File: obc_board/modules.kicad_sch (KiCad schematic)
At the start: 26 parts, among them J10 FSI-110-03-X-D-AD-SD-K-TR, J9 FSI-110-03-X-D-AD-SD-K-TR, U11 LTC4304CMSTRPBF, U12 LTC4304CMSTRPBF

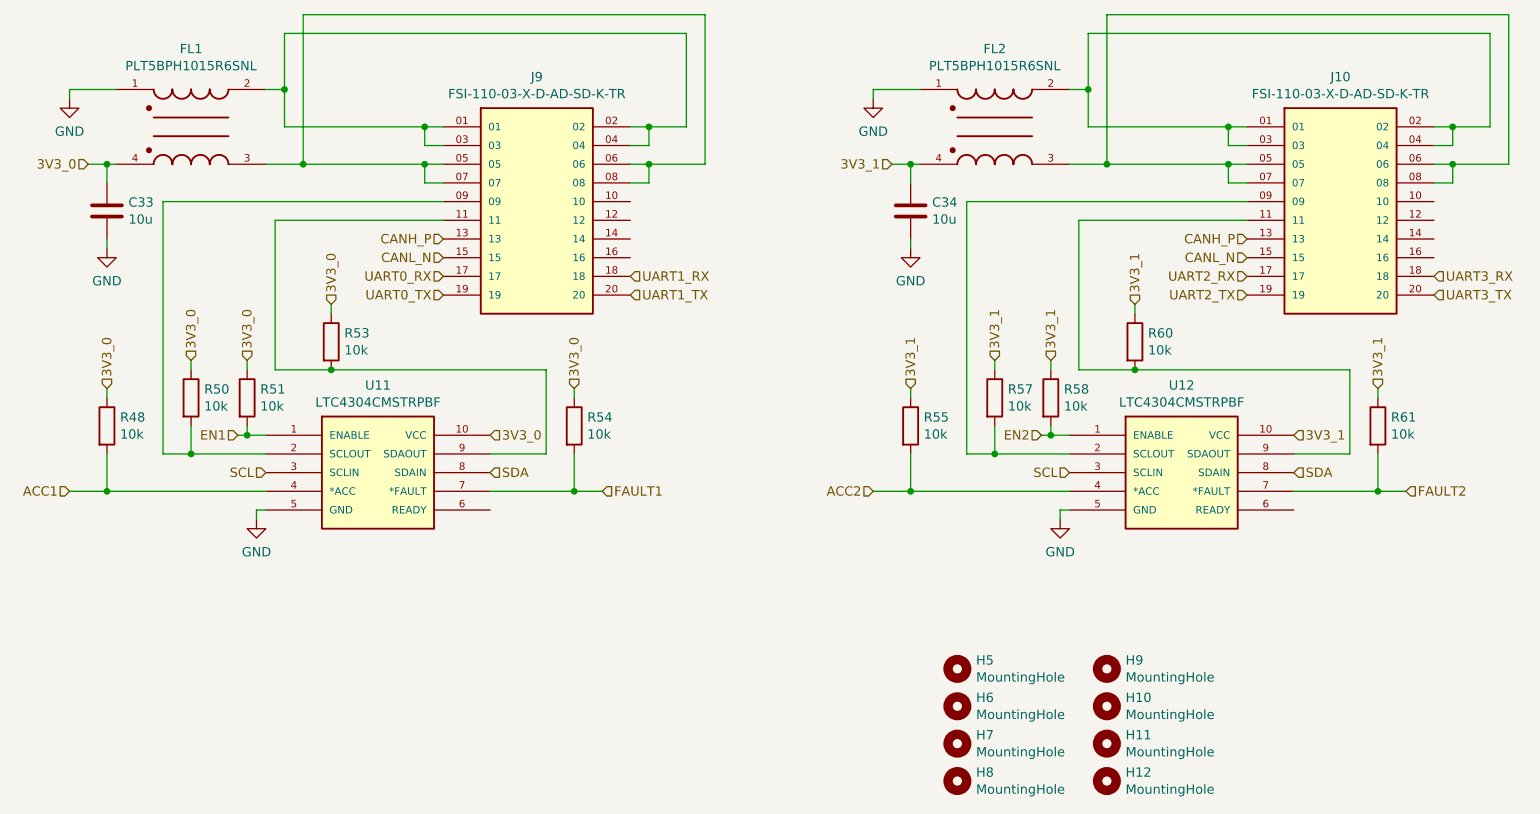
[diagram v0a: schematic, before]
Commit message: changed magnetorquer driver IC and changed power switch IC
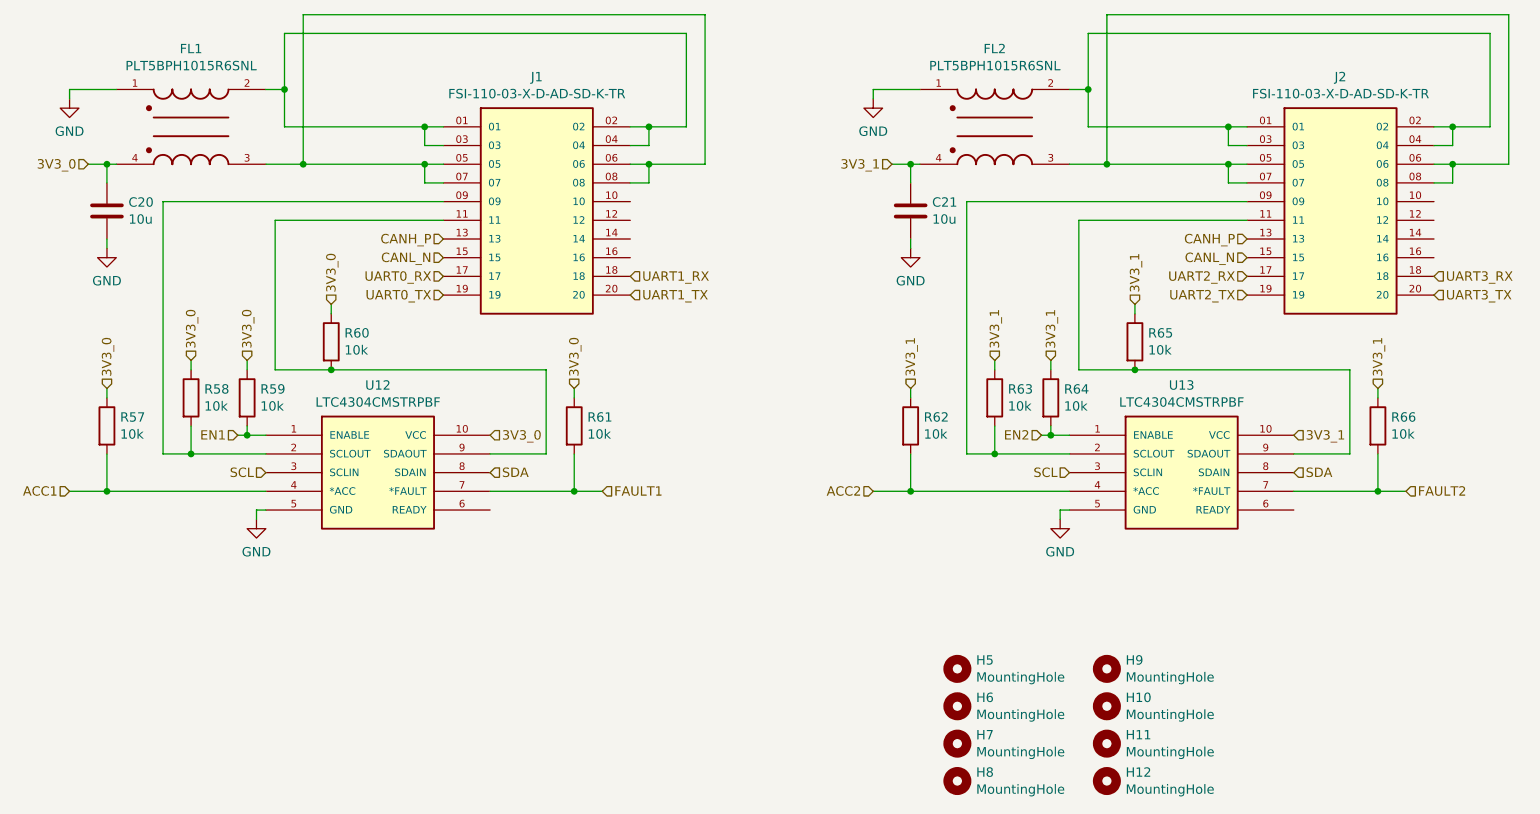
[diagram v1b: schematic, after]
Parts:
- renumbered C33 to C20, C34 to C21, J9 to J1, J10 to J2, R48 to R57, R50 to R58, R51 to R59, R53 to R60, R54 to R61, R55 to R62, R57 to R63, R58 to R64, R60 to R65, R61 to R66, U11 to U12, U12 to U13
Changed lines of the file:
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@@
   (symbol (lib_id "cubesat_obc_lib:FSI-110-03-X-D-AD-SD-K-TR") (at 115.57 76.2 0) (unit 1)
     (in_bom yes) (on_board yes)
-    (property "Reference" "J9" (id 0) (at 115.57 56.7182 0))
+    (property "Reference" "J1" (id 0) (at 115.57 56.7182 0))
     (property "Value" "FSI-110-03-X-D-AD-SD-K-TR" (id 1) (at 115.57 59.0296 0))
     (property "Footprint" "SAMTEC_FSI-110-03-X-D-AD-SD-K-TR" (id 2) (at 115.57 76.2 0)
@@
   (symbol (lib_id "Device:C") (at 57.15 74.93 0) (unit 1)
     (in_bom yes) (on_board yes)
-    (property "Reference" "C33" (id 0) (at 60.071 73.7616 0)
+    (property "Reference" "C20" (id 0) (at 60.071 73.7616 0)
       (effects (font (size 1.27 1.27)) (justify left))
     )
@@
   (symbol (lib_id "cubesat_obc_lib:LTC4304CMSTRPBF") (at 54.61 106.68 0) (unit 1)
     (in_bom yes) (on_board yes)
-    (property "Reference" "U11" (id 0) (at 93.98 98.6282 0))
+    (property "Reference" "U12" (id 0) (at 93.98 98.6282 0))
     (property "Value" "LTC4304CMSTRPBF" (id 1) (at 93.98 100.9396 0))
     (property "Footprint" "MSOP-10_MS" (id 2) (at 78.74 105.41 0)
@@
   (symbol (lib_id "Device:R") (at 76.2 100.33 0) (unit 1)
     (in_bom yes) (on_board yes)
-    (property "Reference" "R51" (id 0) (at 77.978 99.1616 0)
+    (property "Reference" "R59" (id 0) (at 77.978 99.1616 0)
       (effects (font (size 1.27 1.27)) (justify left))
     )
@@
   (symbol (lib_id "Device:R") (at 57.15 104.14 0) (unit 1)
     (in_bom yes) (on_board yes)
-    (property "Reference" "R48" (id 0) (at 58.928 102.9716 0)
+    (property "Reference" "R57" (id 0) (at 58.928 102.9716 0)
       (effects (font (size 1.27 1.27)) (justify left))
     )
@@
   (symbol (lib_id "Device:R") (at 120.65 104.14 0) (unit 1)
     (in_bom yes) (on_board yes)
-    (property "Reference" "R54" (id 0) (at 122.428 102.9716 0)
+    (property "Reference" "R61" (id 0) (at 122.428 102.9716 0)
       (effects (font (size 1.27 1.27)) (justify left))
     )
@@
   (symbol (lib_id "Device:R") (at 87.63 92.71 0) (unit 1)
     (in_bom yes) (on_board yes)
-    (property "Reference" "R53" (id 0) (at 89.408 91.5416 0)
+    (property "Reference" "R60" (id 0) (at 89.408 91.5416 0)
       (effects (font (size 1.27 1.27)) (justify left))
     )
@@
   (symbol (lib_id "Device:R") (at 68.58 100.33 0) (unit 1)
     (in_bom yes) (on_board yes)
-    (property "Reference" "R50" (id 0) (at 70.358 99.1616 0)
+    (property "Reference" "R58" (id 0) (at 70.358 99.1616 0)
       (effects (font (size 1.27 1.27)) (justify left))
     )
@@
   (symbol (lib_id "cubesat_obc_lib:FSI-110-03-X-D-AD-SD-K-TR") (at 224.79 76.2 0) (unit 1)
     (in_bom yes) (on_board yes)
-    (property "Reference" "J10" (id 0) (at 224.79 56.7182 0))
+    (property "Reference" "J2" (id 0) (at 224.79 56.7182 0))
     (property "Value" "FSI-110-03-X-D-AD-SD-K-TR" (id 1) (at 224.79 59.0296 0))
     (property "Footprint" "SAMTEC_FSI-110-03-X-D-AD-SD-K-TR" (id 2) (at 224.79 76.2 0)
@@
   (symbol (lib_id "Device:C") (at 166.37 74.93 0) (unit 1)
     (in_bom yes) (on_board yes)
-    (property "Reference" "C34" (id 0) (at 169.291 73.7616 0)
+    (property "Reference" "C21" (id 0) (at 169.291 73.7616 0)
       (effects (font (size 1.27 1.27)) (justify left))
     )
@@
   (symbol (lib_id "cubesat_obc_lib:LTC4304CMSTRPBF") (at 163.83 106.68 0) (unit 1)
     (in_bom yes) (on_board yes)
-    (property "Reference" "U12" (id 0) (at 203.2 98.6282 0))
+    (property "Reference" "U13" (id 0) (at 203.2 98.6282 0))
     (property "Value" "LTC4304CMSTRPBF" (id 1) (at 203.2 100.9396 0))
     (property "Footprint" "MSOP-10_MS" (id 2) (at 187.96 105.41 0)
@@
   (symbol (lib_id "Device:R") (at 185.42 100.33 0) (unit 1)
     (in_bom yes) (on_board yes)
-    (property "Reference" "R58" (id 0) (at 187.198 99.1616 0)
+    (property "Reference" "R64" (id 0) (at 187.198 99.1616 0)
       (effects (font (size 1.27 1.27)) (justify left))
     )
@@
   (symbol (lib_id "Device:R") (at 166.37 104.14 0) (unit 1)
     (in_bom yes) (on_board yes)
-    (property "Reference" "R55" (id 0) (at 168.148 102.9716 0)
+    (property "Reference" "R62" (id 0) (at 168.148 102.9716 0)
       (effects (font (size 1.27 1.27)) (justify left))
     )
@@
   (symbol (lib_id "Device:R") (at 229.87 104.14 0) (unit 1)
     (in_bom yes) (on_board yes)
-    (property "Reference" "R61" (id 0) (at 231.648 102.9716 0)
+    (property "Reference" "R66" (id 0) (at 231.648 102.9716 0)
       (effects (font (size 1.27 1.27)) (justify left))
     )
@@
   (symbol (lib_id "Device:R") (at 196.85 92.71 0) (unit 1)
     (in_bom yes) (on_board yes)
-    (property "Reference" "R60" (id 0) (at 198.628 91.5416 0)
+    (property "Reference" "R65" (id 0) (at 198.628 91.5416 0)
       (effects (font (size 1.27 1.27)) (justify left))
     )
@@
   (symbol (lib_id "Device:R") (at 177.8 100.33 0) (unit 1)
     (in_bom yes) (on_board yes)
-    (property "Reference" "R57" (id 0) (at 179.578 99.1616 0)
+    (property "Reference" "R63" (id 0) (at 179.578 99.1616 0)
       (effects (font (size 1.27 1.27)) (justify left))
     )
@@
   (symbol (lib_id "power:GND") (at 166.37 80.01 0) (unit 1)
     (in_bom yes) (on_board yes) (fields_autoplaced)
-    (property "Reference" "#PWR?" (id 0) (at 166.37 86.36 0)
+    (property "Reference" "#PWR038" (id 0) (at 166.37 86.36 0)
       (effects (font (size 1.27 1.27)) hide)
     )
@@
   (symbol (lib_id "power:GND") (at 57.15 80.01 0) (unit 1)
     (in_bom yes) (on_board yes) (fields_autoplaced)
-    (property "Reference" "#PWR?" (id 0) (at 57.15 86.36 0)
+    (property "Reference" "#PWR035" (id 0) (at 57.15 86.36 0)
       (effects (font (size 1.27 1.27)) hide)
     )
@@
   (symbol (lib_id "power:GND") (at 77.47 116.84 0) (unit 1)
     (in_bom yes) (on_board yes) (fields_autoplaced)
-    (property "Reference" "#PWR?" (id 0) (at 77.47 123.19 0)
+    (property "Reference" "#PWR036" (id 0) (at 77.47 123.19 0)
       (effects (font (size 1.27 1.27)) hide)
     )
@@
   (symbol (lib_id "power:GND") (at 52.07 59.69 0) (unit 1)
     (in_bom yes) (on_board yes) (fields_autoplaced)
-    (property "Reference" "#PWR?" (id 0) (at 52.07 66.04 0)
+    (property "Reference" "#PWR034" (id 0) (at 52.07 66.04 0)
       (effects (font (size 1.27 1.27)) hide)
     )
@@
   (symbol (lib_id "power:GND") (at 186.69 116.84 0) (unit 1)
     (in_bom yes) (on_board yes) (fields_autoplaced)
-    (property "Reference" "#PWR?" (id 0) (at 186.69 123.19 0)
+    (property "Reference" "#PWR039" (id 0) (at 186.69 123.19 0)
       (effects (font (size 1.27 1.27)) hide)
     )
@@
   (symbol (lib_id "power:GND") (at 161.29 59.69 0) (unit 1)
     (in_bom yes) (on_board yes) (fields_autoplaced)
-    (property "Reference" "#PWR?" (id 0) (at 161.29 66.04 0)
-      (effects (font (size 1.27 1.27)) hide)
-    )
+    (property "Reference" "#PWR037" (id 0) (at 161.29 66.04 0)
+      (effects (font (size 1.27 1.27)) hide)
+    )

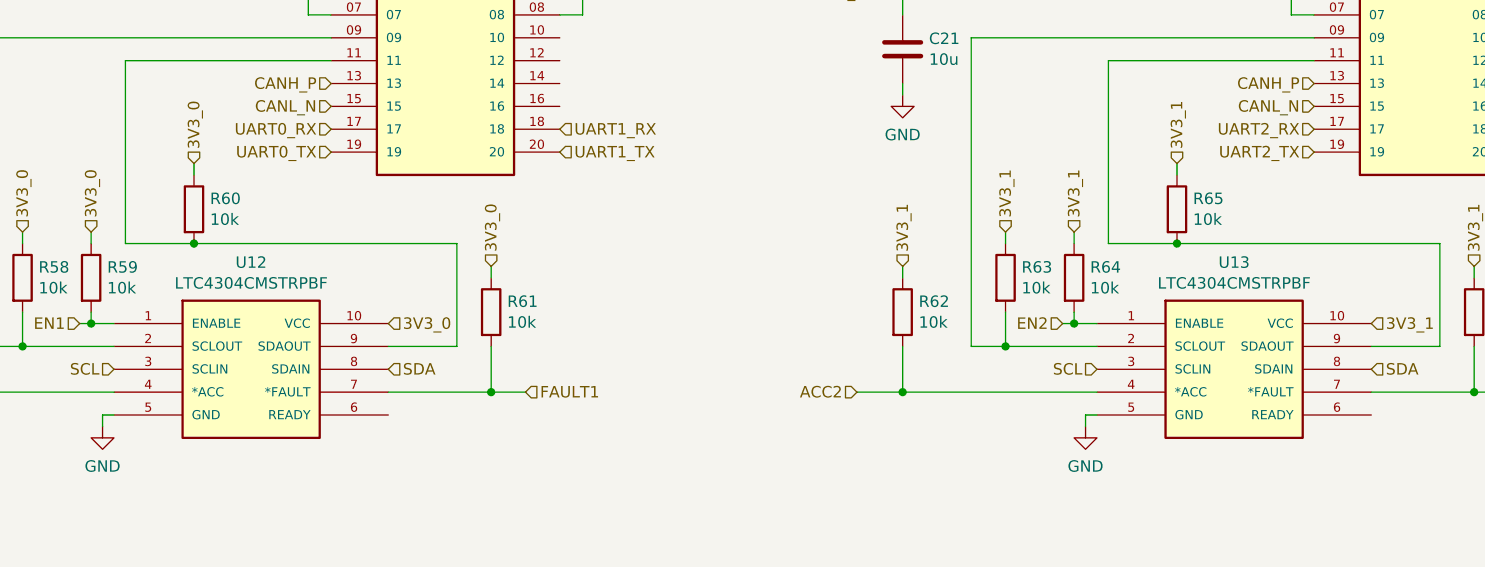
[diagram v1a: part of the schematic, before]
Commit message: updated digikey part numbers and footprints
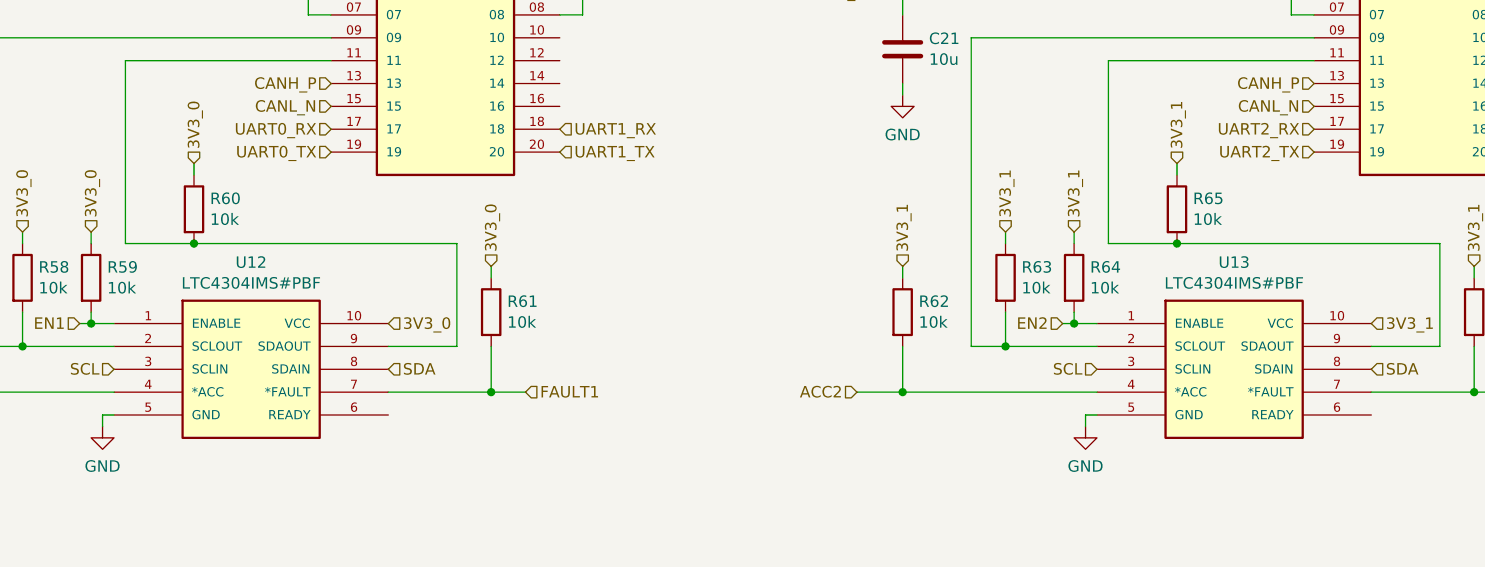
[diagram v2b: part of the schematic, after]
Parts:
- C20, C21: Digikey Part Number 311-1952-1-ND -> 399-7012-1-ND
- R57, R58, R59, R60, R61, R62, R63, R64, R65, R66: Digikey Part Number 311-10.0KLRCT-ND -> YAG3436CT-ND
- U12, U13: value LTC4304CMSTRPBF -> LTC4304IMS#PBF; Digikey Part Number LTC4304CMS#PBF-ND -> LTC4304IMS#PBF-ND
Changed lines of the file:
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@@
       (effects (font (size 1.27 1.27)) hide)
     )
-    (property "Digikey Part Number" "311-1952-1-ND" (id 4) (at 57.15 74.93 0)
+    (property "Digikey Part Number" "399-7012-1-ND" (id 4) (at 57.15 74.93 0)
       (effects (font (size 1.27 1.27)) hide)
     )
@@
     (in_bom yes) (on_board yes)
     (property "Reference" "U12" (id 0) (at 93.98 98.6282 0))
-    (property "Value" "LTC4304CMSTRPBF" (id 1) (at 93.98 100.9396 0))
+    (property "Value" "LTC4304IMS#PBF" (id 1) (at 93.98 100.9396 0))
     (property "Footprint" "MSOP-10_MS" (id 2) (at 78.74 105.41 0)
       (effects (font (size 1.27 1.27)) (justify left bottom) hide)
     )
-    (property "Datasheet" "ltc4304cms#trpbf" (id 3) (at 78.74 105.41 0)
+    (property "Datasheet" "https://www.analog.com/media/en/technical-documentation/data-sheets/4304fa.pdf" (id 3) (at 78.74 105.41 0)
       (effects (font (size 1.27 1.27)) (justify left bottom) hide)
     )
@@
       (effects (font (size 1.27 1.27)) (justify left bottom) hide)
     )
-    (property "Digikey Part Number" "LTC4304CMS#PBF-ND" (id 5) (at 54.61 106.68 0)
+    (property "Digikey Part Number" "LTC4304IMS#PBF-ND" (id 5) (at 54.61 106.68 0)
       (effects (font (size 1.27 1.27)) hide)
     )
@@
       (effects (font (size 1.27 1.27)) hide)
     )
-    (property "Digikey Part Number" "311-10.0KLRCT-ND" (id 4) (at 76.2 100.33 0)
+    (property "Digikey Part Number" "YAG3436CT-ND" (id 4) (at 76.2 100.33 0)
       (effects (font (size 1.27 1.27)) hide)
     )
@@
       (effects (font (size 1.27 1.27)) hide)
     )
-    (property "Digikey Part Number" "311-10.0KLRCT-ND" (id 4) (at 57.15 104.14 0)
+    (property "Digikey Part Number" "YAG3436CT-ND" (id 4) (at 57.15 104.14 0)
       (effects (font (size 1.27 1.27)) hide)
     )
@@
       (effects (font (size 1.27 1.27)) hide)
     )
-    (property "Digikey Part Number" "311-10.0KLRCT-ND" (id 4) (at 120.65 104.14 0)
+    (property "Digikey Part Number" "YAG3436CT-ND" (id 4) (at 120.65 104.14 0)
       (effects (font (size 1.27 1.27)) hide)
     )
@@
       (effects (font (size 1.27 1.27)) hide)
     )
-    (property "Digikey Part Number" "311-10.0KLRCT-ND" (id 4) (at 87.63 92.71 0)
+    (property "Digikey Part Number" "YAG3436CT-ND" (id 4) (at 87.63 92.71 0)
       (effects (font (size 1.27 1.27)) hide)
     )
@@
       (effects (font (size 1.27 1.27)) hide)
     )
-    (property "Digikey Part Number" "311-10.0KLRCT-ND" (id 4) (at 68.58 100.33 0)
+    (property "Digikey Part Number" "YAG3436CT-ND" (id 4) (at 68.58 100.33 0)
       (effects (font (size 1.27 1.27)) hide)
     )
@@
       (effects (font (size 1.27 1.27)) hide)
     )
-    (property "Digikey Part Number" "311-1952-1-ND" (id 4) (at 166.37 74.93 0)
+    (property "Digikey Part Number" "399-7012-1-ND" (id 4) (at 166.37 74.93 0)
       (effects (font (size 1.27 1.27)) hide)
     )
@@
     (in_bom yes) (on_board yes)
     (property "Reference" "U13" (id 0) (at 203.2 98.6282 0))
-    (property "Value" "LTC4304CMSTRPBF" (id 1) (at 203.2 100.9396 0))
+    (property "Value" "LTC4304IMS#PBF" (id 1) (at 203.2 100.9396 0))
     (property "Footprint" "MSOP-10_MS" (id 2) (at 187.96 105.41 0)
       (effects (font (size 1.27 1.27)) (justify left bottom) hide)
     )
-    (property "Datasheet" "ltc4304cms#trpbf" (id 3) (at 187.96 105.41 0)
+    (property "Datasheet" "https://www.analog.com/media/en/technical-documentation/data-sheets/4304fa.pdf" (id 3) (at 187.96 105.41 0)
       (effects (font (size 1.27 1.27)) (justify left bottom) hide)
     )
@@
       (effects (font (size 1.27 1.27)) (justify left bottom) hide)
     )
-    (property "Digikey Part Number" "LTC4304CMS#PBF-ND" (id 5) (at 163.83 106.68 0)
+    (property "Digikey Part Number" "LTC4304IMS#PBF-ND" (id 5) (at 163.83 106.68 0)
       (effects (font (size 1.27 1.27)) hide)
     )
@@
       (effects (font (size 1.27 1.27)) hide)
     )
-    (property "Digikey Part Number" "311-10.0KLRCT-ND" (id 4) (at 185.42 100.33 0)
+    (property "Digikey Part Number" "YAG3436CT-ND" (id 4) (at 185.42 100.33 0)
       (effects (font (size 1.27 1.27)) hide)
     )
@@
       (effects (font (size 1.27 1.27)) hide)
     )
-    (property "Digikey Part Number" "311-10.0KLRCT-ND" (id 4) (at 166.37 104.14 0)
+    (property "Digikey Part Number" "YAG3436CT-ND" (id 4) (at 166.37 104.14 0)
       (effects (font (size 1.27 1.27)) hide)
     )
@@
       (effects (font (size 1.27 1.27)) hide)
     )
-    (property "Digikey Part Number" "311-10.0KLRCT-ND" (id 4) (at 229.87 104.14 0)
+    (property "Digikey Part Number" "YAG3436CT-ND" (id 4) (at 229.87 104.14 0)
       (effects (font (size 1.27 1.27)) hide)
     )
@@
       (effects (font (size 1.27 1.27)) hide)
     )
-    (property "Digikey Part Number" "311-10.0KLRCT-ND" (id 4) (at 196.85 92.71 0)
+    (property "Digikey Part Number" "YAG3436CT-ND" (id 4) (at 196.85 92.71 0)
       (effects (font (size 1.27 1.27)) hide)
     )
@@
       (effects (font (size 1.27 1.27)) hide)
     )
-    (property "Digikey Part Number" "311-10.0KLRCT-ND" (id 4) (at 177.8 100.33 0)
-      (effects (font (size 1.27 1.27)) hide)
-    )
+    (property "Digikey Part Number" "YAG3436CT-ND" (id 4) (at 177.8 100.33 0)
+      (effects (font (size 1.27 1.27)) hide)
+    )
